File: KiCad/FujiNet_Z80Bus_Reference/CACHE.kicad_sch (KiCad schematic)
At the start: 6 parts, among them IC13 7432N, IC15 7408N, IC6 74590N, IC7 74590N

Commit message: Massive fix to KiCad Labels
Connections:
- net CACHE_SEL_3: no longer IC15.3 (O)
- net LOCAL_ADD_0 renamed LOCAL_A0
- net LOCAL_ADD_1 renamed LOCAL_A1
- net LOCAL_ADD_10 renamed LOCAL_A10
- net LOCAL_ADD_11 renamed LOCAL_A11
- net LOCAL_ADD_12 renamed LOCAL_A12
- net LOCAL_ADD_2 renamed LOCAL_A2
- net LOCAL_ADD_3 renamed LOCAL_A3
- net LOCAL_ADD_4 renamed LOCAL_A4
- net LOCAL_ADD_5 renamed LOCAL_A5
- net LOCAL_ADD_6 renamed LOCAL_A6
- net LOCAL_ADD_7 renamed LOCAL_A7
- net LOCAL_ADD_8 renamed LOCAL_A8
- net LOCAL_ADD_9 renamed LOCAL_A9
- net LOCAL_DATA_0 renamed LOCAL_D0
- net LOCAL_DATA_1 renamed LOCAL_D1
- net LOCAL_DATA_2 renamed LOCAL_D2
- net LOCAL_DATA_3 renamed LOCAL_D3
- net LOCAL_DATA_4 renamed LOCAL_D4
- net LOCAL_DATA_5 renamed LOCAL_D5
- net LOCAL_DATA_6 renamed LOCAL_D6
- net LOCAL_DATA_7 renamed LOCAL_D7
- net LOCAL_IORQ renamed LOCAL_CONTROL.IORQ
- net LOCAL_MEMRQ renamed LOCAL_CONTROL.MEMRQ
- net LOCAL_RD renamed LOCAL_CONTROL.RD
- net LOCAL_WR renamed LOCAL_CONTROL.WR
- net Z80_RD renamed Z80_CONTROL.RD
- net Z80_WR renamed Z80_CONTROL.WR
- new net LOCAL_ADD_16: IC15.3 (O)
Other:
- moved on the sheet: IC13B, IC15A, IC15B, IC15C, IC15D, IC6A, IC7A

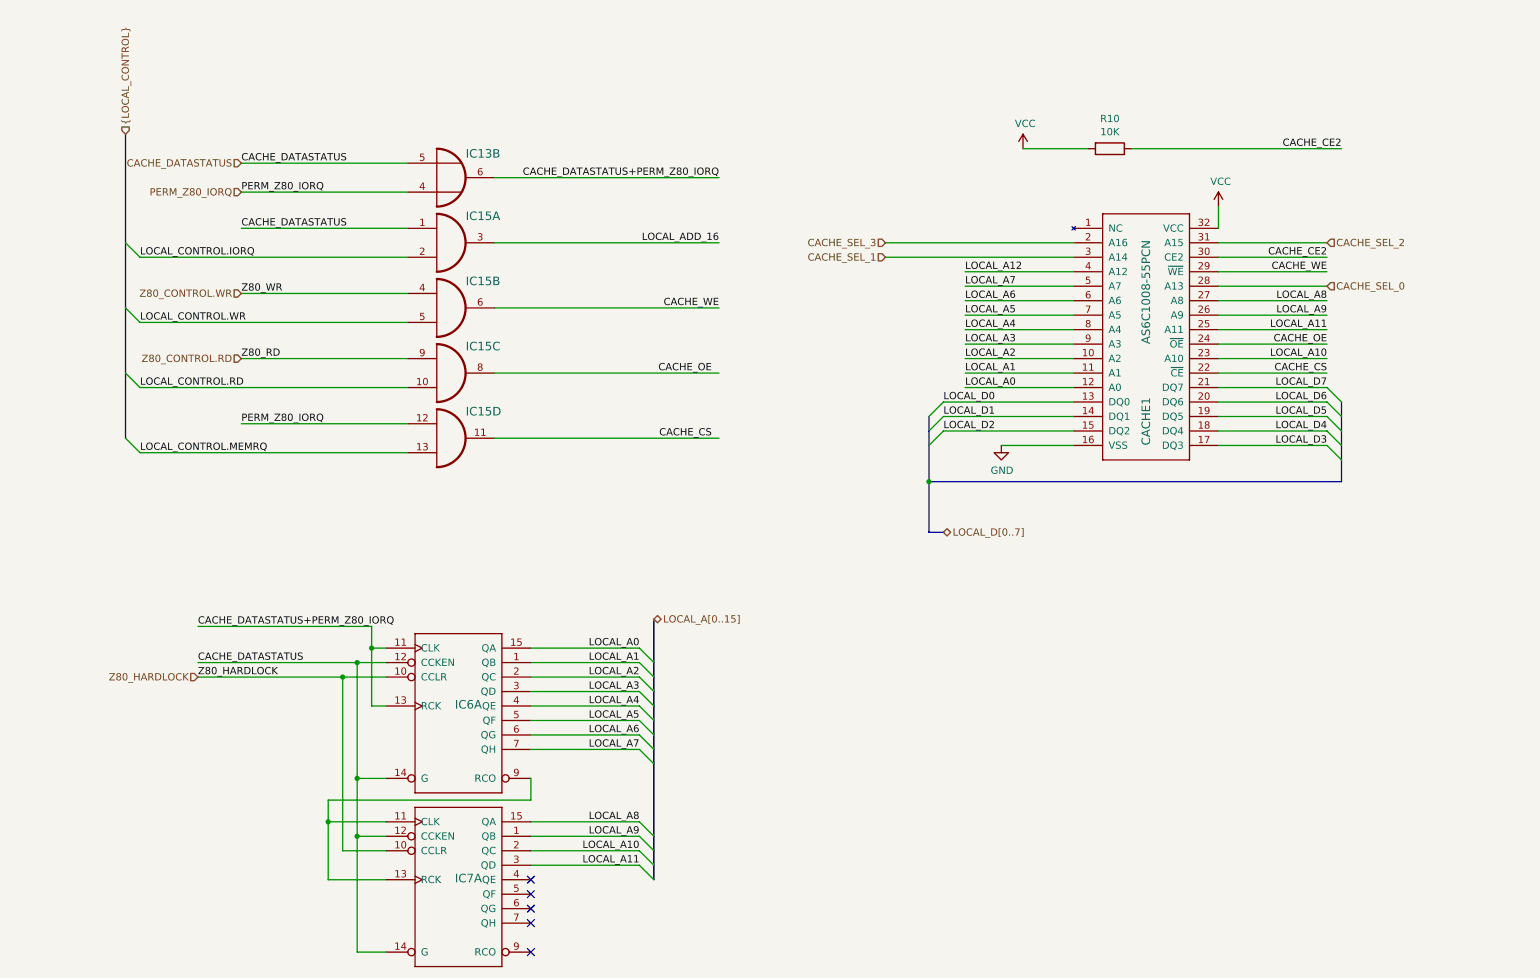
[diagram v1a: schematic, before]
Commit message: KiCad Labels mostly fixed
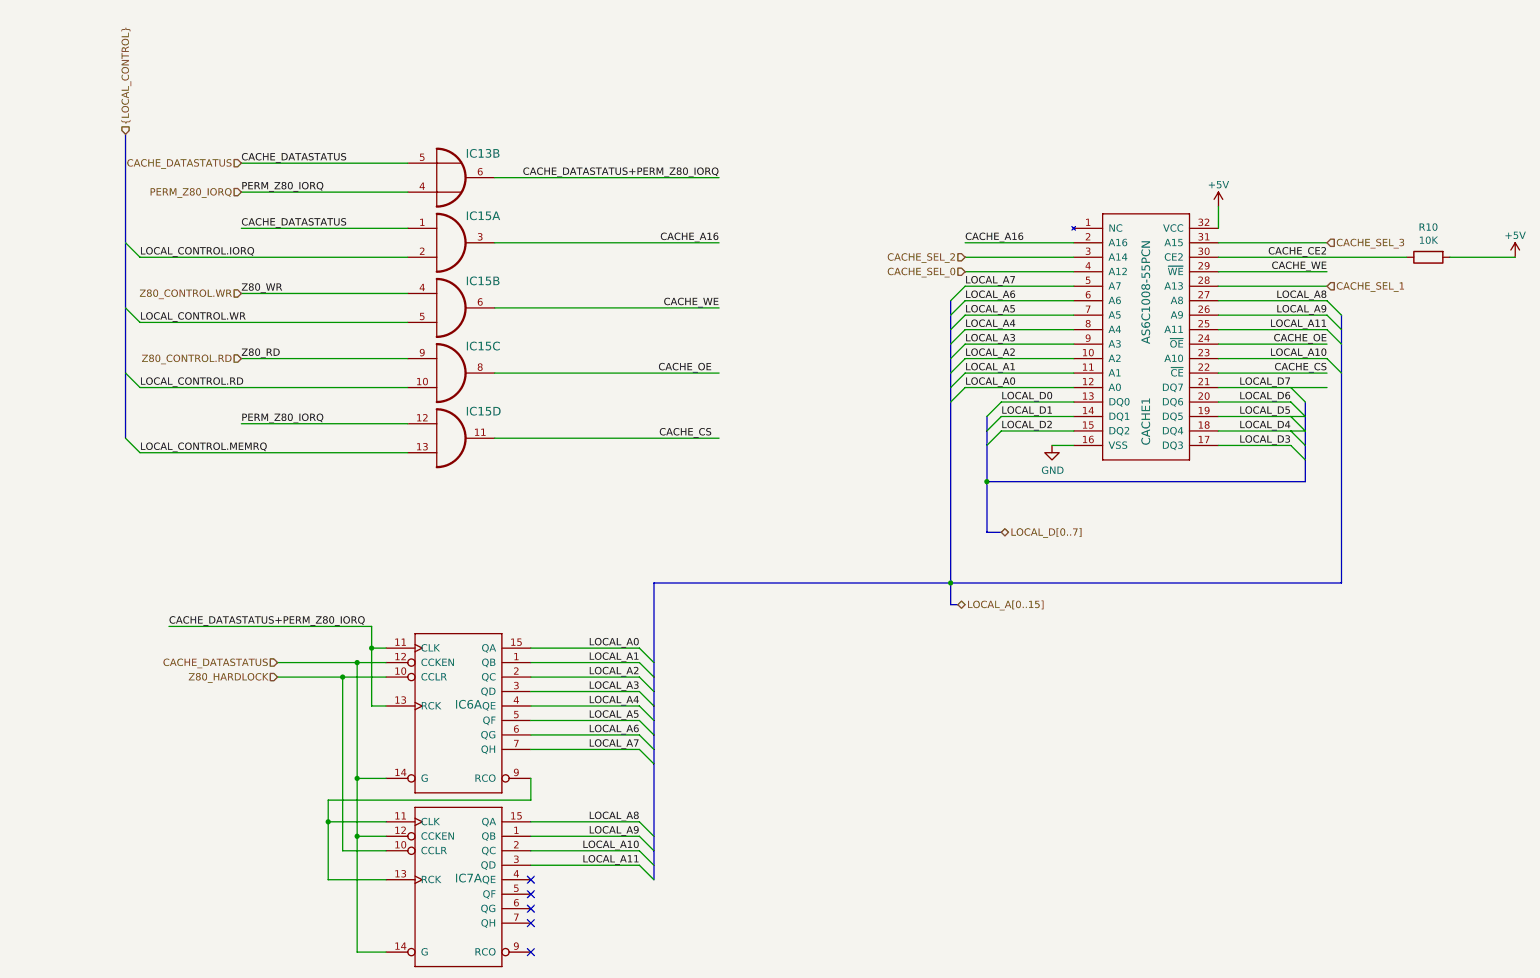
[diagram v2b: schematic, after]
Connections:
- net LOCAL_A12 is gone; now on net CACHE_SEL_0: CACHE1.4 (A12)
- net CACHE_SEL_0: no longer CACHE1.28 (A13)
- net CACHE_SEL_1: now also CACHE1.28 (A13); no longer CACHE1.3 (A14)
- net CACHE_SEL_2: now also CACHE1.3 (A14); no longer CACHE1.31 (A15)
- net CACHE_SEL_3: now also CACHE1.31 (A15); no longer CACHE1.2 (A16)
- net LOCAL_ADD_16 renamed CACHE_A16
- net CACHE_A16: now also CACHE1.2 (A16)
- net VCC renamed +5V
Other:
- moved on the sheet: R10
